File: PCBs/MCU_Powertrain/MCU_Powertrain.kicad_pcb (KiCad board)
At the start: 4 copper layers, 135 x 54 mm, 157 parts, among them J1 PHASE_A, J2 PHASE_B, J3 PHASE_C, J4 Big Conn, J5 Pogo Conn, J6 Conn CAN, J7 PWRIN, Q1 SIZF906DT, Q2 SIZF906DT, Q3 SIZF906DT, SW1 SW_Push, SW2 SW_Push, U1 DRV8305, U2 SN65HVD232, U3 MCP2515, U4 LMR16006XDDC, U5 TMS320F28027F, U6 SN74LVC2G07, U7 SN74LVC2G07, Y1 20MHz

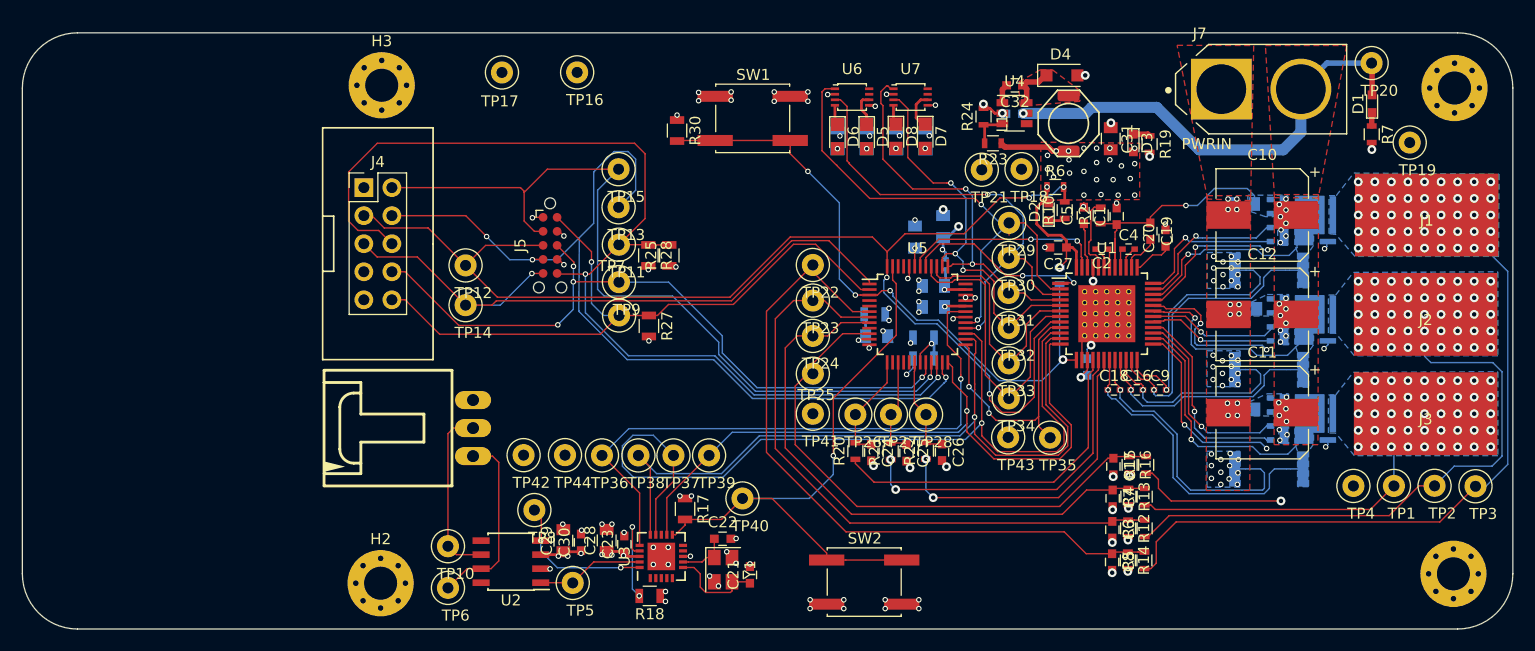
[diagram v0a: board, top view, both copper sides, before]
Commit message: Countour and CAN
- Shrunk board outline
- Swapped out CAN tranciever
- Added 5V LDO for CAN outputs, CAN now 5V compatible
- Checked over layout
- Everything finished except silkscreen
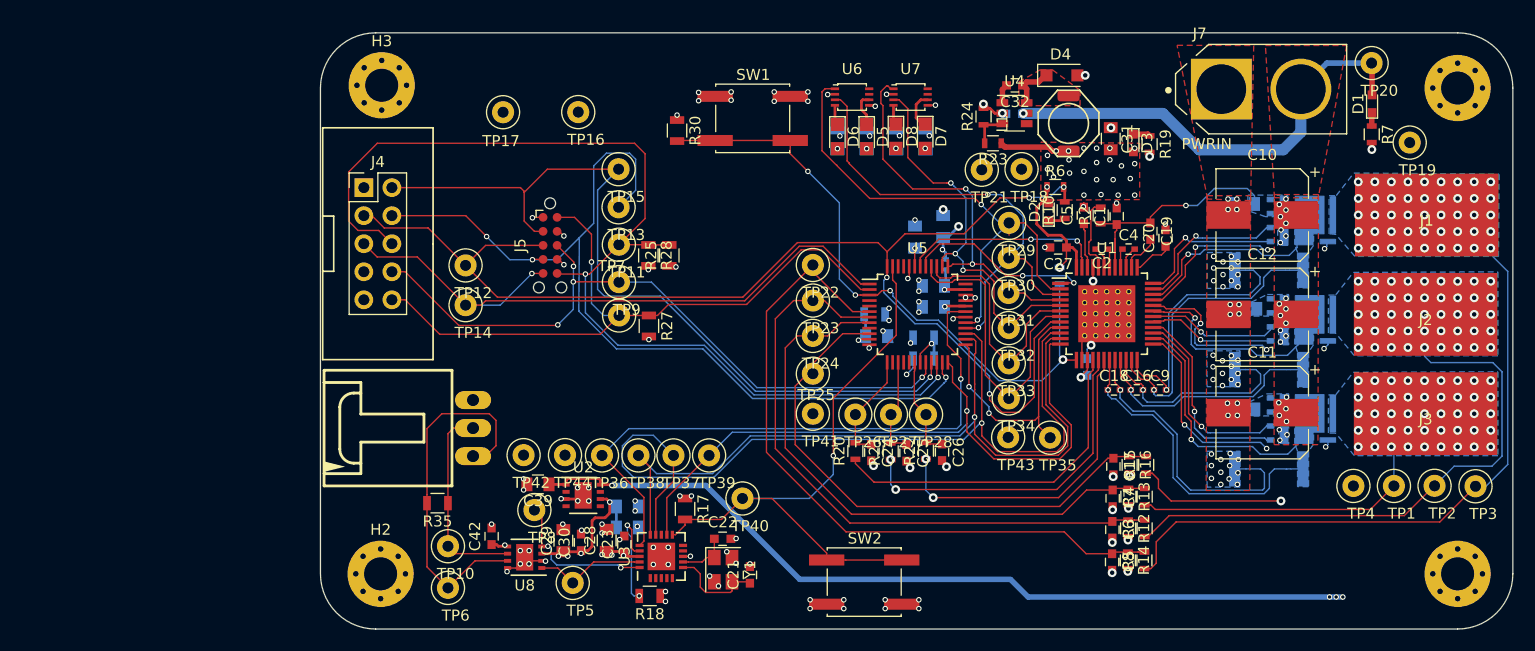
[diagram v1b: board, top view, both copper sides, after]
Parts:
- added C39: 1uF, Capacitors_SMD:C_0805, F.Cu at (23.7, 117.9)
- added C40: 1uF, Capacitors_SMD:C_0805, B.Cu at (31.8, 121.8)
- added C41: 1uF, Capacitors_SMD:C_0805, B.Cu at (31.8, 119.9)
- added C42: 0.1uF, Capacitors_SMD:C_0603, F.Cu at (19.5, 122.6)
- added R35: 120, Resistors_SMD:R_0805, F.Cu at (14.6, 119.6)
- added U8: MCP2562, Housings_DFN_QFN:DFN-8-1EP_3x3mm_Pitch0.65mm, F.Cu at (22.5, 124.5)
- U2: value SN65HVD232 -> RTQ2569-50GQW; footprint Housings_SOIC:SOIC-8_3.9x4.9mm_Pitch1.27mm -> Housings_DFN_QFN:DFN-8-1EP_3x3mm_Pitch0.65mm
- moved U2 8.88 mm to (27.8, 118.9), turned to 0 degrees
- moved TP16 3.60 mm to (27.4, 84.2)
- moved TP17 3.60 mm to (20.5, 84.2)
- moved H2 0.85 mm to (9.45, 126.0)
- moved H1 0.38 mm to (107.0, 126.0)
- moved H4 0.28 mm to (107.0, 82.0)
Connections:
- C29 pad 1: +3V3 -> +5V
- C30 pad 1: +3V3 -> +5V
- U2 pad 1: /TXCAN -> +BATT
- U2 pad 2: GND -> Net-(U2-Pad2)
- U2 pad 3: +3V3 -> GND
- U2 pad 4: /RXCAN -> Net-(U2-Pad4)
- U2 pad 6: /CANL -> +5V
- U2 pad 7: /CANH -> Net-(U2-Pad7)
- U2 pad 8: Net-(U2-Pad8) -> +BATT
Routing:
- net +BATT: track 78.8 -> 183.9 mm, vias 27 -> 31
- net /CANH: track 17.1 -> 33.5 mm
- net +5V: track 0.00 -> 14.1 mm, vias 0 -> 4
- net GND: track 37.0 -> 41.7 mm, vias 123 -> 139
- net /CANL: track 16.0 -> 18.4 mm
- net +3V3: track 37.3 -> 35.2 mm, vias 49 -> 47
- net /RXCAN: track 13.6 -> 14.7 mm
- net Net-(R18-Pad2): track 9.25 -> 10.2 mm
- net /TDI: track 63.8 -> 62.9 mm
- net /TMS: track 74.5 -> 73.9 mm
- net /GPIO29: track 60.5 -> 59.9 mm
- net /TRST: track 61.7 -> 62.2 mm
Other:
- board size 135 x 54 mm -> 108 x 54 mm
- rule via_min_size: 0.4 -> 0.3

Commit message: Silkscreen
- Finished up silkscreen
- Checked routing, looks good
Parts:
- J7: value PWRIN -> PWR_IN
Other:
- board text added: "+V_IN"
- board text added: "120 Ohm Termination"
- board text added: "3V3"
- board text added: "5V"
- board text added: "CANBUS"
- board text added: "CANH"
- board text added: "CANL"
- board text added: "CAN_INT"
- board text added: "CAN_INT_TEST"
- board text added: "CH"
- board text added: "CL"
- board text added: "EPWM 1A"
- board text added: "EPWM 1B"
- board text added: "EPWM 2A"
- board text added: "EPWM 2B"
- board text added: "EPWM 3A"
- board text added: "EPWM 3B"
- board text added: "FOC Motor Controller Dev. Board"
- board text added: "GND"
- board text added: "GPIO28"
- board text added: "GPIO29"
- board text added: "I_A"
- board text added: "I_B"
- board text added: "I_C"
- board text added: "JTAG PROGRAMMING"
- board text added: "Mark Belbin -- 2020"
- board text added: "PH_A"
- board text added: "PH_B"
- board text added: "PH_C"
- board text added: "RESET"
- board text added: "RXCAN"
- board text added: "SPI_CLK"
- board text added: "SPI_CS_0"
- board text added: "SPI_CS_1"
- board text added: "SPI_MISO"
- board text added: "SPI_MOSI"
- board text added: "TCK"
- board text added: "TDI"
- board text added: "TDO"
- board text added: "TMS"
- board text added: "TRST"
- board text added: "TXCAN"
- board text added: "V_A"
- board text added: "V_B"
- board text added: "V_BUS"
- board text added: "V_C"

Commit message: Gerbers + Planes
- Added extra mid layer planes for heatsinking
- Generated gerbers
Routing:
- net +BATT: track 183.9 -> 156.6 mm
- added copper zone on In1.Cu, net /Powertrain/Phase_A
- added copper zone on In2.Cu, net /Powertrain/Phase_A
- added copper zone on In1.Cu, net /Powertrain/Phase_B
- added copper zone on In2.Cu, net /Powertrain/Phase_B
- added copper zone on In1.Cu, net /Powertrain/Phase_C
- added copper zone on In2.Cu, net /Powertrain/Phase_C
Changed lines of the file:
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@@
     (thickness 1.6)
     (drawings 72)
-    (tracks 1682)
+    (tracks 1681)
     (zones 0)
     (modules 163)
@@
   (layers
     (0 F.Cu signal)
-    (1 In1.Cu power hide)
-    (2 In2.Cu power hide)
+    (1 In1.Cu power)
+    (2 In2.Cu power)
     (31 B.Cu signal)
-    (32 B.Adhes user hide)
-    (33 F.Adhes user hide)
-    (34 B.Paste user hide)
-    (35 F.Paste user hide)
+    (32 B.Adhes user)
+    (33 F.Adhes user)
+    (34 B.Paste user)
+    (35 F.Paste user)
     (36 B.SilkS user)
     (37 F.SilkS user)
@@
     (visible_elements 7FFFFFFF)
     (pcbplotparams
-      (layerselection 0x010fc_ffffffff)
-      (usegerberextensions false)
+      (layerselection 0x010f0_ffffffff)
+      (usegerberextensions true)
       (usegerberattributes false)
       (usegerberadvancedattributes false)
@@
       (outputformat 1)
       (mirror false)
-      (drillshape 1)
+      (drillshape 0)
       (scaleselection 1)
-      (outputdirectory ""))
+      (outputdirectory "Gerbers/"))
   )
   (net 0 "")
@@
   (segment (start 30.325 117.925) (end 30.4 118) (width 0.25) (layer F.Cu) (net 1))
   (via (at 96.6 128.1) (size 0.5) (drill 0.3) (layers F.Cu B.Cu) (net 1))
-  (segment (start 68.1 128.1) (end 95.4 128.1) (width 0.25) (layer B.Cu) (net 1))
   (segment (start 96 128.1) (end 96.6 128.1) (width 0.25) (layer B.Cu) (net 1))
   (via (at 96 128.1) (size 0.5) (drill 0.3) (layers F.Cu B.Cu) (net 1))
@@
   (segment (start 92.8 86.000401) (end 91.200401 87.6) (width 1) (layer B.Cu) (net 1))
   (segment (start 92.8 82.1) (end 92.8 86.000401) (width 1) (layer B.Cu) (net 1))
-  (segment (start 68.1 128.1) (end 66.55 126.55) (width 0.5) (layer B.Cu) (net 1))
   (segment (start 96.6 128.1) (end 68.1 128.1) (width 0.5) (layer B.Cu) (net 1))
   (segment (start 66.5 126.5) (end 66.55 126.55) (width 0.25) (layer B.Cu) (net 1))
@@
   (segment (start 47.403998 126.5) (end 38.903998 118) (width 0.5) (layer B.Cu) (net 1))
   (segment (start 66.5 126.5) (end 47.403998 126.5) (width 0.5) (layer B.Cu) (net 1))
+  (segment (start 68.1 128.1) (end 66.55 126.55) (width 0.5) (layer B.Cu) (net 1))
   (via (at 86.4 115.1) (size 0.5) (drill 0.3) (layers F.Cu B.Cu) (net 2))
   (via (at 87.15 115.65) (size 0.5) (drill 0.3) (layers F.Cu B.Cu) (net 2))
@@
       )
     )
+  )
+  (zone (net 44) (net_name /Powertrain/Phase_A) (layer In1.Cu) (hatch edge 0.508)
+    (priority 1)
+    (connect_pads yes (clearance 0.2))
+    (min_thickness 0.254)
+    (fill yes (arc_segments 32) (thermal_gap 0.508) (thermal_bridge_width 0.508) (smoothing fillet) (radius 0.25))
+    (polygon
+      (pts
+        (xy 110.65 97.225) (xy 97.6125 97.2) (xy 97.6375 89.725) (xy 110.725 89.725)
+      )
+    )
+  )
+  (zone (net 45) (net_name /Powertrain/Phase_B) (layer In1.Cu) (hatch edge 0.508)
+    (priority 1)
+    (connect_pads yes (clearance 0.2))
+    (min_thickness 0.254)
+    (fill yes (arc_segments 32) (thermal_gap 0.508) (thermal_bridge_width 0.508) (smoothing fillet) (radius 0.25))
+    (polygon
+      (pts
+        (xy 110.608816 106.25) (xy 97.571316 106.225) (xy 97.596316 98.75) (xy 110.683816 98.75)
+      )
+    )
+  )
+  (zone (net 46) (net_name /Powertrain/Phase_C) (layer In1.Cu) (hatch edge 0.508)
+    (priority 1)
+    (connect_pads yes (clearance 0.2))
+    (min_thickness 0.254)
+    (fill yes (arc_segments 32) (thermal_gap 0.508) (thermal_bridge_width 0.508) (smoothing fillet) (radius 0.25))
+    (polygon
+      (pts
+        (xy 110.621127 115.275) (xy 97.583627 115.25) (xy 97.608627 107.775) (xy 110.696127 107.775)
+      )
+    )
+  )
+  (zone (net 46) (net_name /Powertrain/Phase_C) (layer In2.Cu) (hatch edge 0.508)
+    (priority 1)
+    (connect_pads yes (clearance 0.2))
+    (min_thickness 0.254)
+    (fill yes (arc_segments 32) (thermal_gap 0.508) (thermal_bridge_width 0.508) (smoothing fillet) (radius 0.25))
+    (polygon
+      (pts
+        (xy 110.5125 115.275) (xy 97.475 115.25) (xy 97.5 107.775) (xy 110.5875 107.775)
+      )
+    )
+  )
+  (zone (net 45) (net_name /Powertrain/Phase_B) (layer In2.Cu) (hatch edge 0.508)
+    (priority 1)
+    (connect_pads yes (clearance 0.2))
+    (min_thickness 0.254)
+    (fill yes (arc_segments 32) (thermal_gap 0.508) (thermal_bridge_width 0.508) (smoothing fillet) (radius 0.25))
+    (polygon
+      (pts
+        (xy 110.545874 106.24) (xy 97.508374 106.215) (xy 97.533374 98.74) (xy 110.620874 98.74)
+      )
+    )
+  )
+  (zone (net 44) (net_name /Powertrain/Phase_A) (layer In2.Cu) (hatch edge 0.508)
+    (priority 1)
+    (connect_pads yes (clearance 0.2))
+    (min_thickness 0.254)
+    (fill yes (arc_segments 32) (thermal_gap 0.508) (thermal_bridge_width 0.508) (smoothing fillet) (radius 0.25))
+    (polygon
+      (pts
+        (xy 110.673552 97.251115) (xy 97.636052 97.226115) (xy 97.661052 89.751115) (xy 110.748552 89.751115)
+      )
+    )
